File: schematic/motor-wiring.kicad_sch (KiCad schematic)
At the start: 25 parts, among them J1 LRS-600, J10 MCU USB, J11 LAPTOP, J2 TB1, J3 TB3, J4 TB2, J5 BLY34 (Hall), J6 BLY34 (Phase), J7 MCU GPIO, J8 WALL PLUG, J9 DC-DC REGULATOR (48V -> TBD), Q2 2N3904, Q3 2N3904, Q4 2N3904, SW1 E-STOP (NC), SW2 AC POWER SWITCH (toggle)

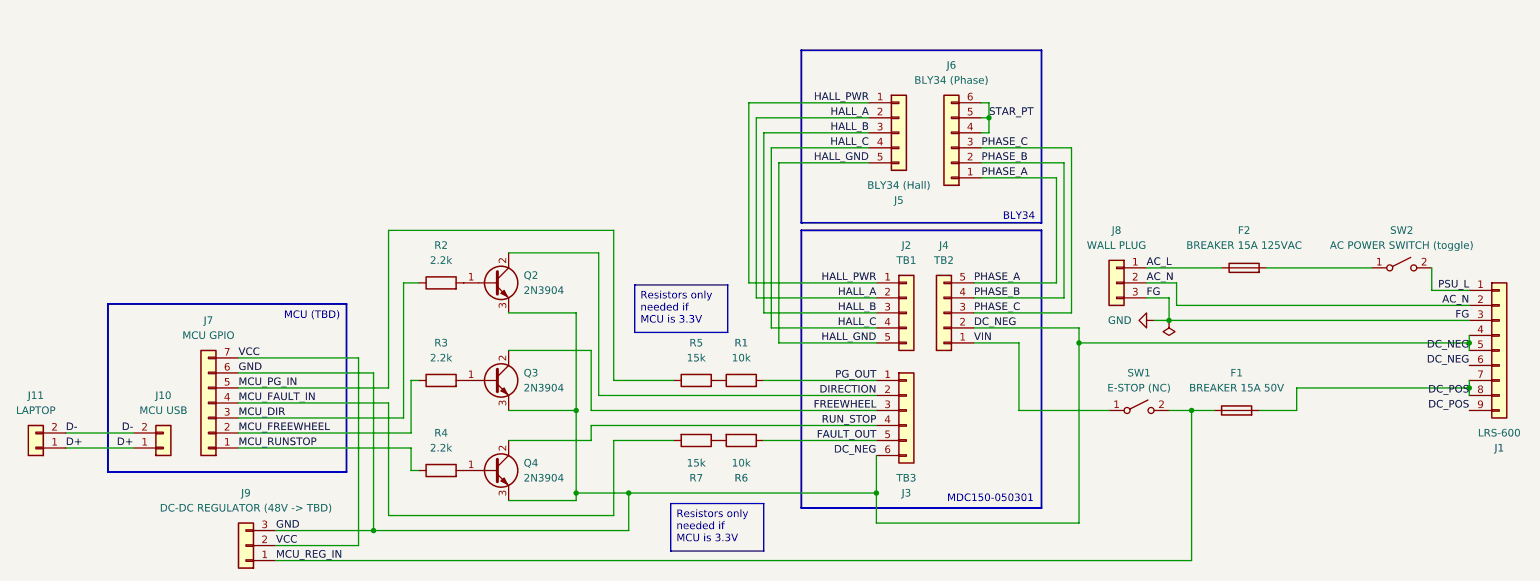
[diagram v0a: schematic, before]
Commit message: Update schematic to match revised plans
- No longer using a DC-DC regulator, instead powering MCU from laptop
- Finalized on Arduino Nano R4 for microcontroller
- Removed voltage dividers, since the R4 runs at 5V
- Updated motor controller to match correct spec sheet (MDC151 instead of MDC150)
- Wired VCONTROL on MCU to motor controller to control speed
- Modeled microcontroller power from laptop USB-C connection
- Removed emergency stop (instead just using AC power toggle) due to complexity at high amperage & voltage
- Removed DC-side breaker
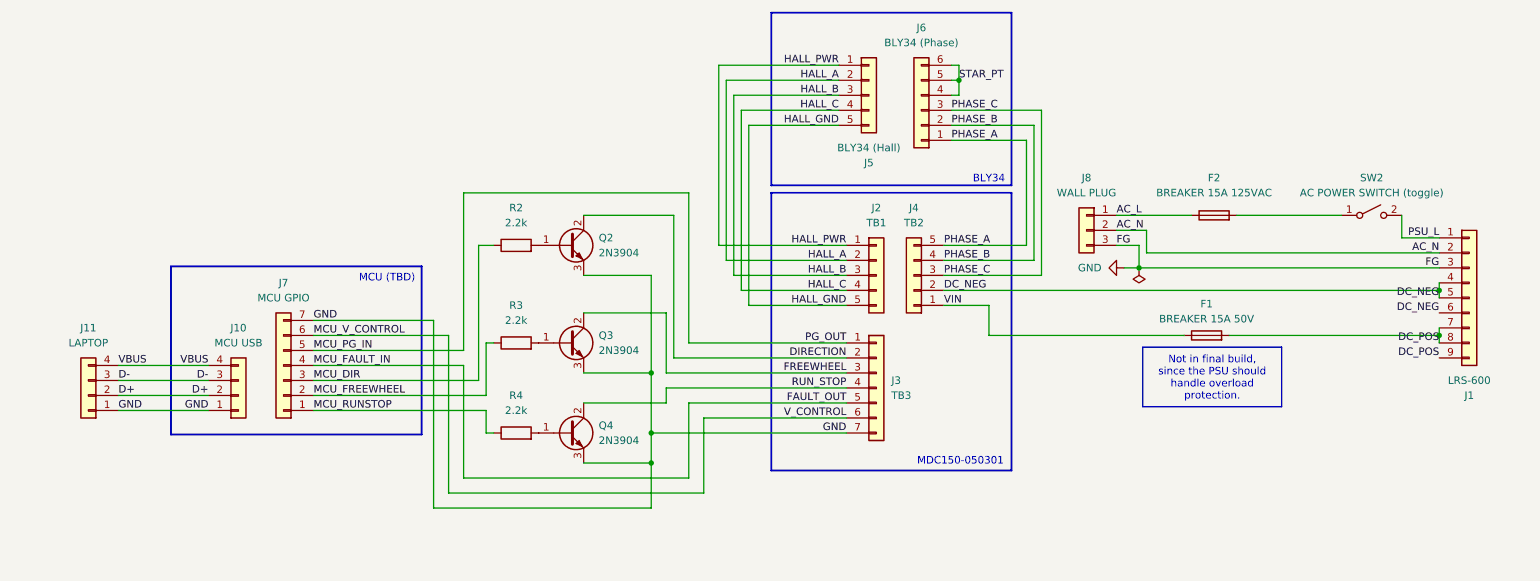
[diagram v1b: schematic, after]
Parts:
- removed J9: DC-DC REGULATOR (48V -> TBD), symbol Connector_Generic:Conn_01x03
- removed R1, R6: 10k, symbol Device:R
- removed R5, R7: 15k, symbol Device:R
- removed SW1: E-STOP (NC), symbol Switch:SW_SPST
- J10, J11: symbol Connector_Generic:Conn_01x02 -> Connector_Generic:Conn_01x04
- J3: symbol Connector_Generic:Conn_01x06 -> Connector_Generic:Conn_01x07
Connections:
- net MCU_FAULT_IN is gone; now on net FAULT_OUT: J7.4 (Pin_4)
- net MCU_REG_IN is gone; now on net VIN: F1.1
- net PG_OUT is gone; now on net MCU_PG_IN: J3.1 (Pin_1)
- net VCC is gone; now on net GND: J7.7 (Pin_7)
- net D+: now also J10.2 (Pin_2), J11.2 (Pin_2); no longer J10.1 (Pin_1), J11.1 (Pin_1)
- net D-: now also J10.3 (Pin_3), J11.3 (Pin_3); no longer J10.2 (Pin_2), J11.2 (Pin_2)
- net GND: now also J10.1 (Pin_1), J11.1 (Pin_1), J3.7 (Pin_7); no longer J1.4 (Pin_4), J1.5 (Pin_5), J1.6 (Pin_6), J3.6 (Pin_6), J4.2 (Pin_2), J7.6 (Pin_6)
- new net DC_NEG: J1.4 (Pin_4), J1.5 (Pin_5), J1.6 (Pin_6), J4.2 (Pin_2)
- new net MCU_V_CONTROL: J3.6 (Pin_6), J7.6 (Pin_6)
- new net VBUS: J10.4 (Pin_4), J11.4 (Pin_4)
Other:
- moved on the sheet: F1, F2, J1, J2, J4, J5, J6, J7, J8, Q2, Q3, Q4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

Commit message: Decide what pins to use on microcontroller
Added annotations
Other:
- note added: "(D2)"
- note added: "(D4)"
- note added: "(D6)"
- note added: "(D7)"
- note added: "(D8)"
- note added: "(D9)"
- note added: "(GND)"
- note added: "Arduino Nano R4"
- note added: "MDC151-050301"
- note removed: "MCU (TBD)"
- note removed: "MDC150-050301"
- moved on the sheet: J10, J11, J7
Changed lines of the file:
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@@
 	)
 	(rectangle
-		(start 46.99 79.756)
-		(end 89.408 108.204)
+		(start 40.64 79.756)
+		(end 88.265 108.204)
 		(stroke
 			(width 0.3048)
@@
 		)
 	)
-	(text "MCU (TBD)"
+	(text "(D2)"
 		(exclude_from_sim no)
-		(at 83.566 81.788 0)
-		(effects
-			(font
-				(size 1.27 1.27)
-			)
+		(at 82.042 96.52 0)
+		(effects
+			(font
+				(size 1.27 1.27)
+			)
+			(justify left bottom)
+		)
+	)
+	(text "Arduino Nano R4 "
+		(exclude_from_sim no)
+		(at 74.422 82.042 0)
+		(effects
+			(font
+				(size 1.27 1.27)
+			)
+		)
+	)
+	(text "(D7)"
+		(exclude_from_sim no)
+		(at 82.042 99.06 0)
+		(effects
+			(font
+				(size 1.27 1.27)
+			)
+			(justify left bottom)
 		)
 	)
@@
 		)
 	)
-	(text "MDC150-050301"
+	(text "(D8)"
+		(exclude_from_sim no)
+		(at 82.042 104.14 0)
+		(effects
+			(font
+				(size 1.27 1.27)
+			)
+			(justify left bottom)
+		)
+	)
+	(text "(GND)"
+		(exclude_from_sim no)
+		(at 81.28 88.9 0)
+		(effects
+			(font
+				(size 1.27 1.27)
+			)
+			(justify left bottom)
+		)
+	)
+	(text "(D6)"
+		(exclude_from_sim no)
+		(at 82.042 101.6 0)
+		(effects
+			(font
+				(size 1.27 1.27)
+			)
+			(justify left bottom)
+		)
+	)
+	(text "(D9)"
+		(exclude_from_sim no)
+		(at 82.042 91.44 0)
+		(effects
+			(font
+				(size 1.27 1.27)
+			)
+			(justify left bottom)
+		)
+	)
+	(text "(D4)"
+		(exclude_from_sim no)
+		(at 82.042 93.98 0)
+		(effects
+			(font
+				(size 1.27 1.27)
+			)
+			(justify left bottom)
+		)
+	)
+	(text "MDC151-050301"
 		(exclude_from_sim no)
 		(at 180.594 112.776 0)
@@
 	(text_box "Not in final build, since the PSU should handle overload protection."
 		(exclude_from_sim no)
-		(at 211.455 93.4228 0)
+		(at 210.82 93.4228 0)
 		(size 23.495 10.0822)
 		(margins 0.9525 0.9525 0.9525 0.9525)
@@
 	(wire
 		(pts
-			(xy 71.12 99.06) (xy 99.06 99.06)
+			(xy 64.77 99.06) (xy 99.06 99.06)
 		)
 		(stroke
@@
 	(wire
 		(pts
-			(xy 100.33 101.6) (xy 71.12 101.6)
+			(xy 100.33 101.6) (xy 64.77 101.6)
 		)
 		(stroke
@@
 	(wire
 		(pts
-			(xy 38.1 104.14) (xy 53.34 104.14)
-		)
-		(stroke
-			(width 0)
-			(type default)
-			(color 0 0 0 1)
-		)
-	)
-	(wire
-		(pts
-			(xy 38.1 96.52) (xy 53.34 96.52)
+			(xy 31.75 104.14) (xy 46.99 104.14)
+		)
+		(stroke
+			(width 0)
+			(type default)
+			(color 0 0 0 1)
+		)
+	)
+	(wire
+		(pts
+			(xy 31.75 96.52) (xy 46.99 96.52)
 		)
 		(stroke
@@
 	(wire
 		(pts
-			(xy 38.1 99.06) (xy 53.34 99.06)
+			(xy 31.75 99.06) (xy 46.99 99.06)
 		)
 		(stroke
@@
 	(wire
 		(pts
-			(xy 38.1 101.6) (xy 53.34 101.6)
+			(xy 31.75 101.6) (xy 46.99 101.6)
 		)
 		(stroke
@@
 	(wire
 		(pts
-			(xy 71.12 91.44) (xy 93.98 91.44)
+			(xy 64.77 91.44) (xy 93.98 91.44)
 		)
 		(stroke
@@
 	(wire
 		(pts
-			(xy 96.52 93.98) (xy 71.12 93.98)
+			(xy 96.52 93.98) (xy 64.77 93.98)
 		)
 		(stroke
@@
 	(wire
 		(pts
-			(xy 96.52 96.52) (xy 71.12 96.52)
+			(xy 96.52 96.52) (xy 64.77 96.52)
 		)
 		(stroke
@@
 	(wire
 		(pts
-			(xy 71.12 88.9) (xy 91.44 88.9)
+			(xy 64.77 88.9) (xy 91.44 88.9)
 		)
 		(stroke
@@
 	(wire
 		(pts
-			(xy 100.33 104.14) (xy 71.12 104.14)
+			(xy 100.33 104.14) (xy 64.77 104.14)
 		)
 		(stroke
@@
 	)
 	(label "GND"
-		(at 38.1 104.14 0)
+		(at 31.75 104.14 0)
 		(effects
 			(font
@@
 	)
 	(label "MCU_FREEWHEEL"
-		(at 71.12 101.6 0)
+		(at 64.77 101.6 0)
 		(effects
 			(font
@@
 	)
 	(label "VBUS"
-		(at 53.34 96.52 180)
+		(at 46.99 96.52 180)
 		(effects
 			(font
@@
 	)
 	(label "D+"
-		(at 38.1 101.6 0)
+		(at 31.75 101.6 0)
 		(effects
 			(font
@@
 	)
 	(label "D-"
-		(at 53.34 99.06 180)
+		(at 46.99 99.06 180)
 		(effects
 			(font
@@
 	)
 	(label "MCU_V_CONTROL"
-		(at 71.12 91.44 0)
+		(at 64.77 91.44 0)
 		(effects
 			(font
@@
 	)
 	(label "D+"
-		(at 53.34 101.6 180)
+		(at 46.99 101.6 180)
 		(effects
 			(font
@@
 	)
 	(label "MCU_RUNSTOP"
-		(at 71.12 104.14 0)
+		(at 64.77 104.14 0)
 		(effects
 			(font
@@
 	)
 	(label "GND"
-		(at 53.34 104.14 180)
+		(at 46.99 104.14 180)
 		(effects
 			(font
@@
 	)
 	(label "GND"
-		(at 71.12 88.9 0)
+		(at 64.77 88.9 0)
 		(effects
 			(font
@@
 	)
 	(label "MCU_DIR"
-		(at 71.12 99.06 0)
+		(at 64.77 99.06 0)
 		(effects
 			(font
@@
 	)
 	(label "MCU_PG_IN"
-		(at 71.12 93.98 0)
+		(at 64.77 93.98 0)
 		(effects
 			(font
@@
 	)
 	(label "D-"
-		(at 38.1 99.06 0)
+		(at 31.75 99.06 0)
 		(effects
 			(font
@@
 	)
 	(label "MCU_FAULT_IN"
-		(at 71.12 96.52 0)
+		(at 64.77 96.52 0)
 		(effects
 			(font
@@
 	)
 	(label "VBUS"
-		(at 38.1 96.52 0)
+		(at 31.75 96.52 0)
 		(effects
 			(font
@@
 	(symbol
 		(lib_id "Connector_Generic:Conn_01x04")
-		(at 33.02 101.6 180)
+		(at 26.67 101.6 180)
 		(unit 1)
 		(body_style 1)
@@
 		(fields_autoplaced yes)
 		(property "Reference" "J11"
-			(at 33.02 90.17 0)
+			(at 26.67 90.17 0)
 			(show_name no)
 			(do_not_autoplace no)
@@
 		)
 		(property "Value" "LAPTOP"
-			(at 33.02 92.71 0)
+			(at 26.67 92.71 0)
 			(show_name no)
 			(do_not_autoplace no)
@@
 		)
 		(property "Footprint" ""
-			(at 33.02 101.6 0)
+			(at 26.67 101.6 0)
 			(hide yes)
 			(show_name no)
@@
 		)
 		(property "Datasheet" ""
-			(at 33.02 101.6 0)
+			(at 26.67 101.6 0)
 			(hide yes)
 			(show_name no)
@@
 		)
 		(property "Description" "Generic connector, single row, 01x04, script generated (kicad-library-utils/schlib/autogen/connector/)"
-			(at 33.02 101.6 0)
+			(at 26.67 101.6 0)
 			(hide yes)
 			(show_name no)
@@
 	(symbol
 		(lib_id "Connector_Generic:Conn_01x04")
-		(at 58.42 101.6 0)
+		(at 52.07 101.6 0)
 		(mirror x)
 		(unit 1)
@@
 		(fields_autoplaced yes)
 		(property "Reference" "J10"
-			(at 58.42 90.17 0)
+			(at 52.07 90.17 0)
 			(show_name no)
 			(do_not_autoplace no)
@@
 		)
 		(property "Value" "MCU USB"
-			(at 58.42 92.71 0)
+			(at 52.07 92.71 0)
 			(show_name no)
 			(do_not_autoplace no)
@@
 		)
 		(property "Footprint" ""
-			(at 58.42 101.6 0)
+			(at 52.07 101.6 0)
 			(hide yes)
 			(show_name no)
@@
 		)
 		(property "Datasheet" ""
-			(at 58.42 101.6 0)
+			(at 52.07 101.6 0)
 			(hide yes)
 			(show_name no)
@@
 		)
 		(property "Description" "Generic connector, single row, 01x04, script generated (kicad-library-utils/schlib/autogen/connector/)"
-			(at 58.42 101.6 0)
+			(at 52.07 101.6 0)
 			(hide yes)
 			(show_name no)
@@
 	(symbol
 		(lib_id "Connector_Generic:Conn_01x07")
-		(at 66.04 96.52 180)
+		(at 59.69 96.52 180)
 		(unit 1)
 		(body_style 1)
@@
 		(fields_autoplaced yes)
 		(property "Reference" "J7"
-			(at 66.04 82.55 0)
+			(at 59.69 82.55 0)
 			(show_name no)
 			(do_not_autoplace no)
@@
 		)
 		(property "Value" "MCU GPIO"
-			(at 66.04 85.09 0)
+			(at 59.69 85.09 0)
 			(show_name no)
 			(do_not_autoplace no)
@@
 		)
 		(property "Footprint" ""
-			(at 66.04 96.52 0)
+			(at 59.69 96.52 0)
 			(hide yes)
 			(show_name no)
@@
 		)
 		(property "Datasheet" ""
-			(at 66.04 96.52 0)
+			(at 59.69 96.52 0)
 			(hide yes)
 			(show_name no)
@@
 		)
 		(property "Description" "Generic connector, single row, 01x07, script generated (kicad-library-utils/schlib/autogen/connector/)"
-			(at 66.04 96.52 0)
+			(at 59.69 96.52 0)
 			(hide yes)
 			(show_name no)
